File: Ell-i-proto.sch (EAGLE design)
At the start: 131 parts, among them J1 PROG, J10 EXT-48V, J11 48V, J2 PWMH, J3 PWR, J4 PWML, J5 ANAL, J6 SPI, J7 COMM, J8 ANAH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

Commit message: > - U3 ja U4 pinnijärjestys on muuttunut
Korjattu lbr:ään ja skemaan.

> - D14 pinnijärjestys muuttunut

Se oli mielestäni jo oikein sekä lbr:ssä ja skemassa.  Tarkistin datasheetistä.  Katsokaa nyt tekin.

> - Uusi Juotostäplä Arduino PWR VIN

En löytänyt.  Mihin tämän siis pitäisi tulla?

> - J10 vaihtoehtoinen liitin

Katsotaan tämä nyt tekemäni commitin jälkeen.

> - Uudet juotostäplät:  SHIELD TP10, NGATE TP3

TP10: done
TP3: done

> - Komponentin tyyppi vaihtunut/ollut Eaglessa väärin: D10, D14, L1, FB1, FB2, FB5, ehkä muitakin, näkyvät varmaan BOM:ista?

Korjasin D14:n valueta muuttamalla.  Kotelo on sama, samoin pinnijärjestys.
D10: komponentti lisätty lbr:ään ja skemaan.  Katsokaa onko ok.
L1 oli jo ok.
FB1, FB2 ja FB5: sama kotelo korjattu value

> Ja aiemmasta mailista: Ainakin seuraavat komponentit pitää kuitenkin vielä vaihtaa oikeiksi:
>
>  J9       RJ-45 liitin

Turo, sinullahan oli tähän jokin.  Voinet sen lisätä sekä lbr:ään että skemaan.

>  Q2       transistori

Q2: vaihdettu value.

>  J10      virtaliitin
>  U5       NCP1117 regulaattori

Oli jo kunnossa.

>  D9,D8    Zener-diodit

D8 oli oikein.
D9: tein zenerille uuden kotelon ja vaihdoin sen.

>  FB1,FB2  kuristimet
>  C31,C40  kondensaattorit

En ehdi nyt enää tehdä tuota C31:n komponenttia lbr:ään.
C40 pitäisi kai vain vaihtaa 0805:ksi.  1uF ei taida olla 0402:na.
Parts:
- added TP10, TP3: TPB1,27, testpad:TPB1,27
- D10: value MURA120T3G -> SS2PH10; device ell-i:MURA120T3G -> ell-i:SS2PH10
- D14: value TLV431A -> TLVH431B
- D9: value (none) -> MMSZ4694; device ell-i:ZENER-SOD323-SOD323 -> ell-i:ZENER-SOD323-123
- FB1, FB2: value (none) -> BLM15A
- FB5: value LQM15 -> BLM15A
- Q2: value BC846ALT1SMD -> MMTBA42
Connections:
- removed net N$11: Q3.G, U6.NGATE
- new net NGATE: Q3.G, TP3.TP, U6.NGATE
- net PE: now also TP10.TP
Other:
- moved on the sheet: J9

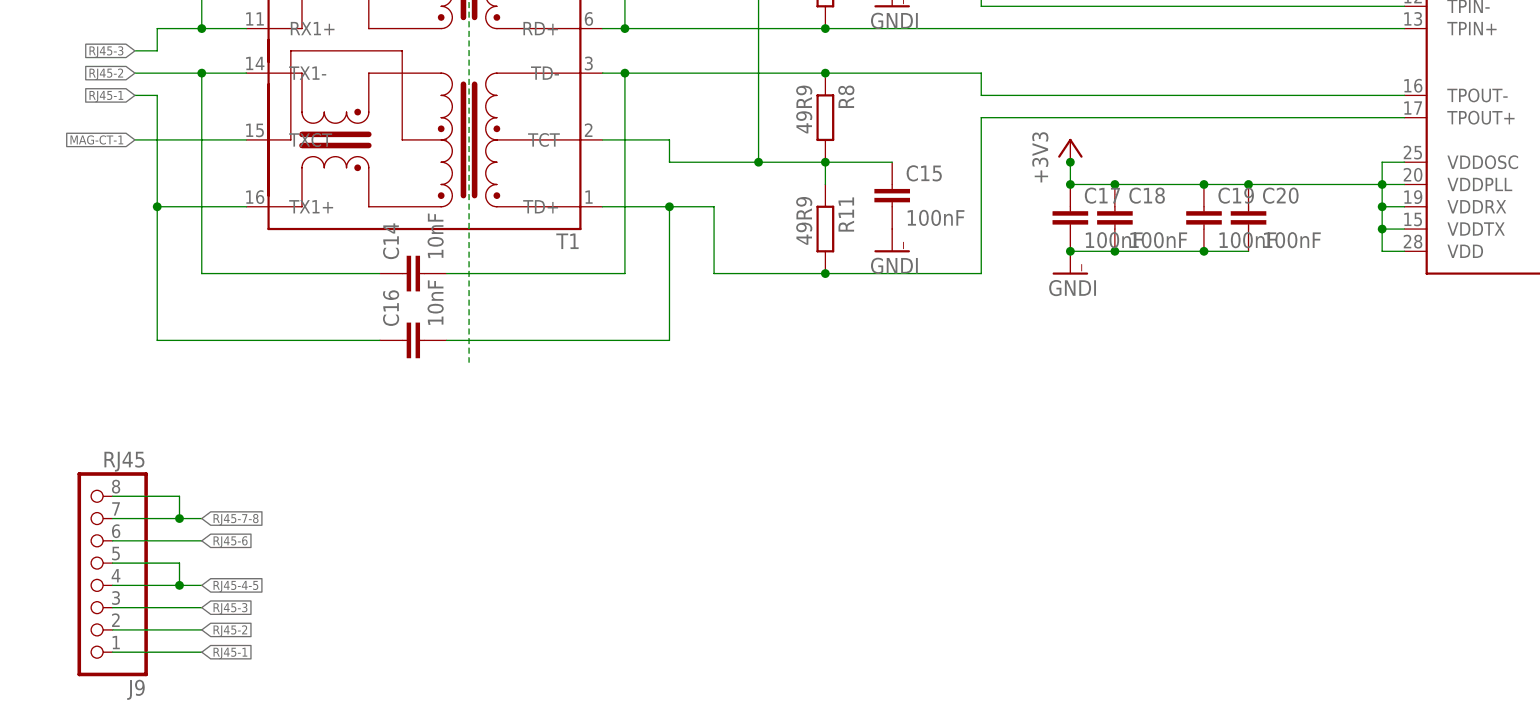
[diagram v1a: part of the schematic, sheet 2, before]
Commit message: library updates, initial state for board, with Arduino Due outline in place
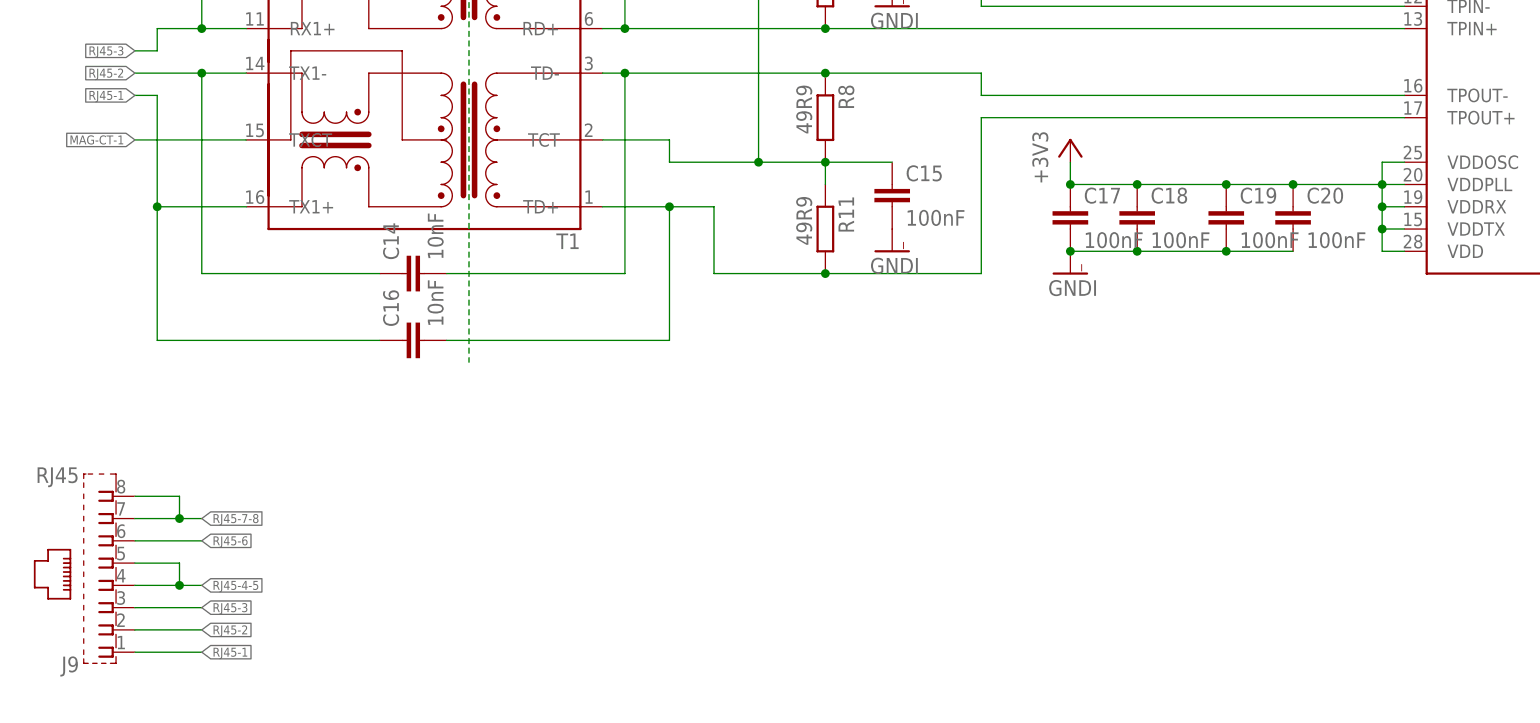
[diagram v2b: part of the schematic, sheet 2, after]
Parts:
- C10, C11, C14, C16, C33, C34: device ell-i:C1206 -> rcl:C-EUC1206
- C26: device ell-i:C1808 -> rcl:C-EUC1206
- C29, C30: device ell-i:C1210 -> rcl:C-EUC1210
- C31: device rcl:CPOL-EU140CLH-0810 -> rcl:CPOL-EU153CLV-0605
- C42: device ell-i:C1812 -> rcl:C-EUC1812
- J10: value EXT-48V -> PJ-102AX; device ell-i:PINHD-1X3 -> ell-i:PJ-102AX
- J9: device ell-i:PINHD-1X8 -> ell-i:43860-0001
- R24: device ell-i:R1206 -> rcl:R-EU_R1206
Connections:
- net GND: now also J10.3; no longer J10.1
- net N184903: now also J10.1; no longer J10.3
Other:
- moved on the sheet: C18, C19, C20, D10, J11

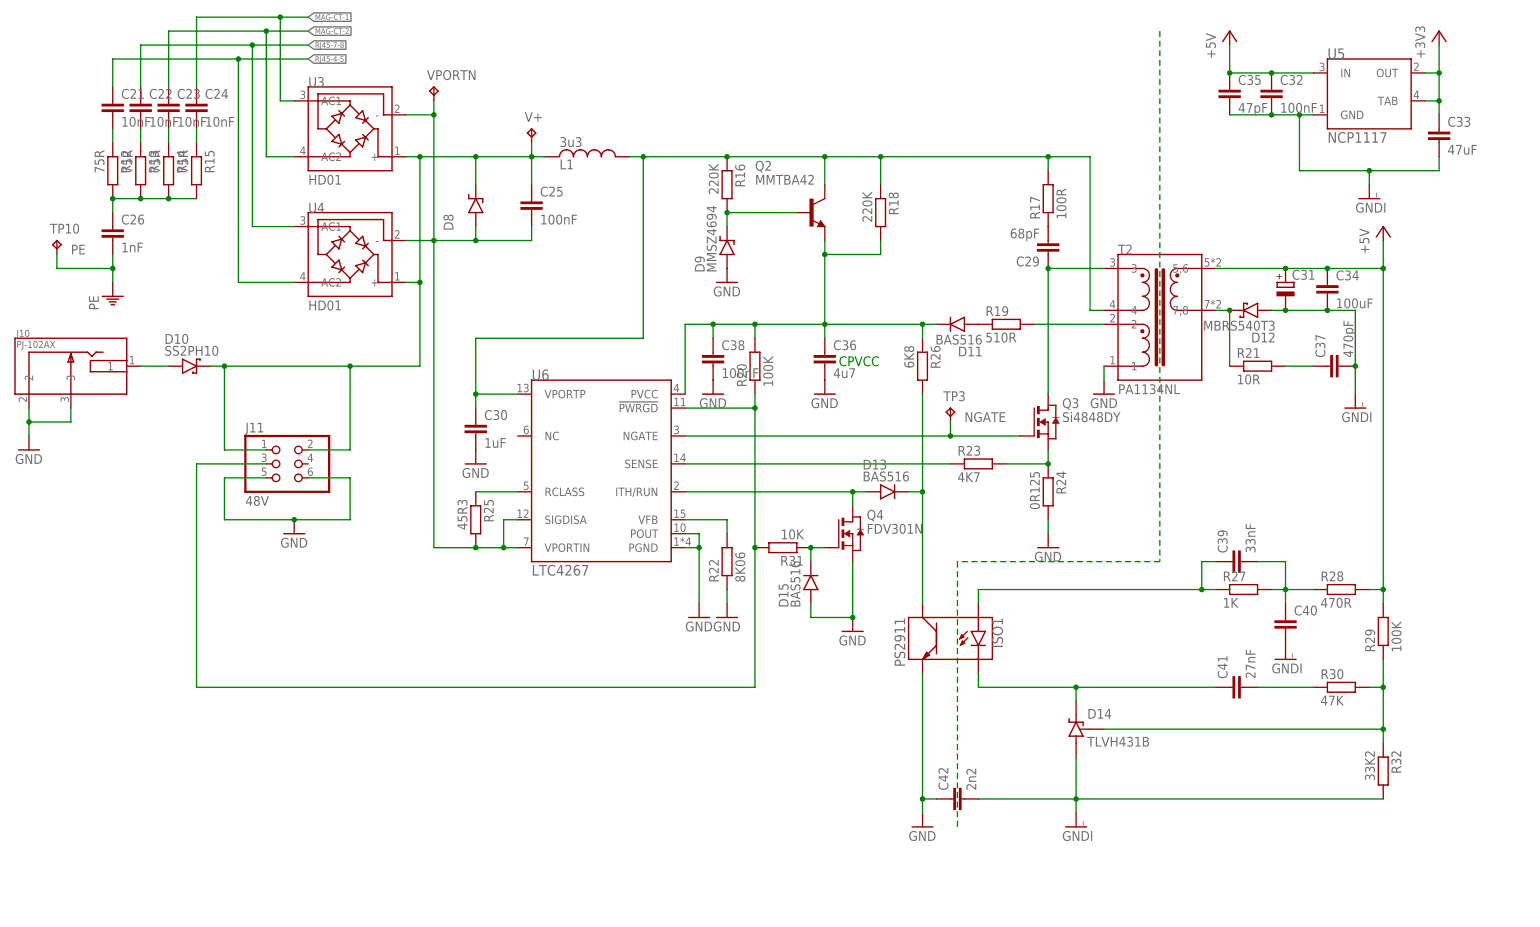
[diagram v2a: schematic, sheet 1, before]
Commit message: mounting holes, S1 & FTDI conn updated, drafting the placements & GND area, etc
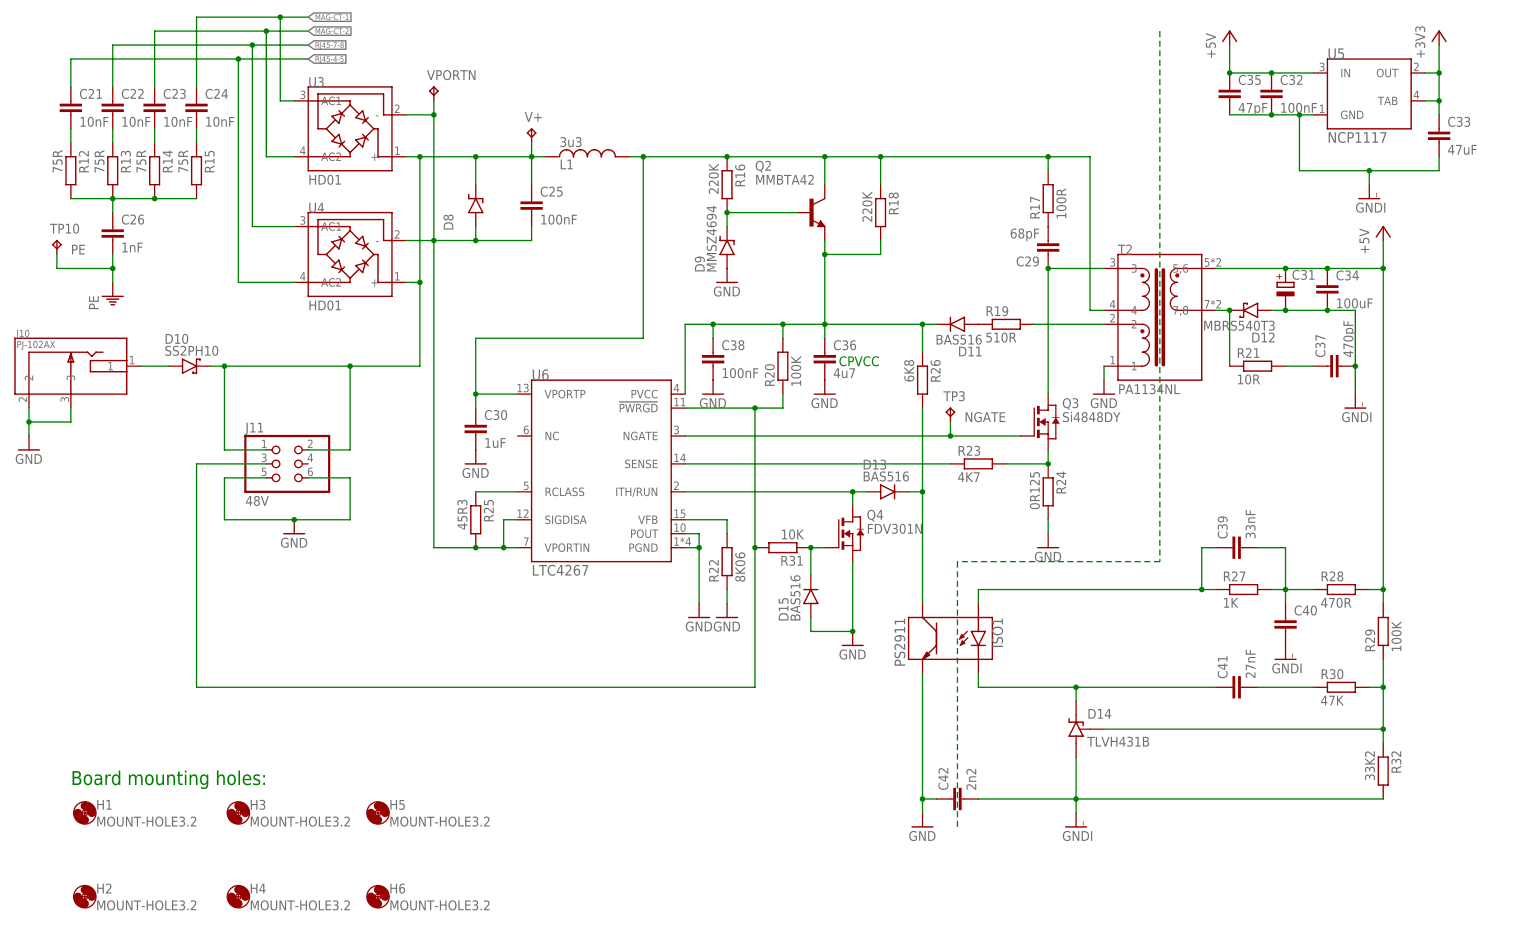
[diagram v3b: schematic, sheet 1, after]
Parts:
- added H1, H2, H3, H4, H5, H6: MOUNT-HOLE3.2, holes:MOUNT-HOLE3.2
- J1: value PROG -> FTDI-SER-6; device ell-i:PINHD-1X6 -> ell-i:FTDI-SER-6
- Q2: value MMTBA42 -> MMBTA42
- S1: value RACON12 -> B3SL-10X2P; device switch-misc:RACON12 -> ell-i:B3SL-10X2P
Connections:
- net GNDI: now also J1.GND; no longer J1.1, S1.P@1
- net N$6: now also J1.-CTS; no longer J1.2
- net NDSR2: now also J1.-RTS; no longer J1.6
- net NRES: no longer S1.S@1
- net RX2: now also J1.TXD; no longer J1.4
- net TX2: now also J1.RXD; no longer J1.5
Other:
- note added: "Board mounting holes:"
- moved on the sheet: C14, C16, C17, C2, C21, C22, C23, C39, C4, D15, D4, D5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
